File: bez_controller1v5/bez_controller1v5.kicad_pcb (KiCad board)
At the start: 4 copper layers, 130 x 65 mm, 88 parts, among them J1 Conn_01x03_Male, J10 Conn_01x07_Socket, J11 Conn_01x03_Male, J12 Conn_01x03_Male, J13 USB_B_Mini, J14 PPTC041LGBN-RC, J15 Conn_01x03_Male, J16 MOLEX_Conn_Button, J17 MOLEX_Conn_Button, J2 Conn_01x03_Male, J3 Conn_01x03_Male, J4 Screw_Terminal_01x02, J5 Conn_01x03_Male, J6 Conn_01x03_Male, J7 Conn_01x03_Male, J8 JTAG Conn_01x06_Male, J9 Conn_01x09_Socket, U10 USBLC6-4SC6, U11 74LVC2G241, U12 74LVC2G241, U2 74LVC2G241, U3 74LVC2G241, U4 LF50ABV_TO220, U5 LD1117AS33TR_SOT223, U6 INA180A1, U7 STM32F446RETx, U8 74LVC2G241, U9 74LVC2G241, Y1 8MHz

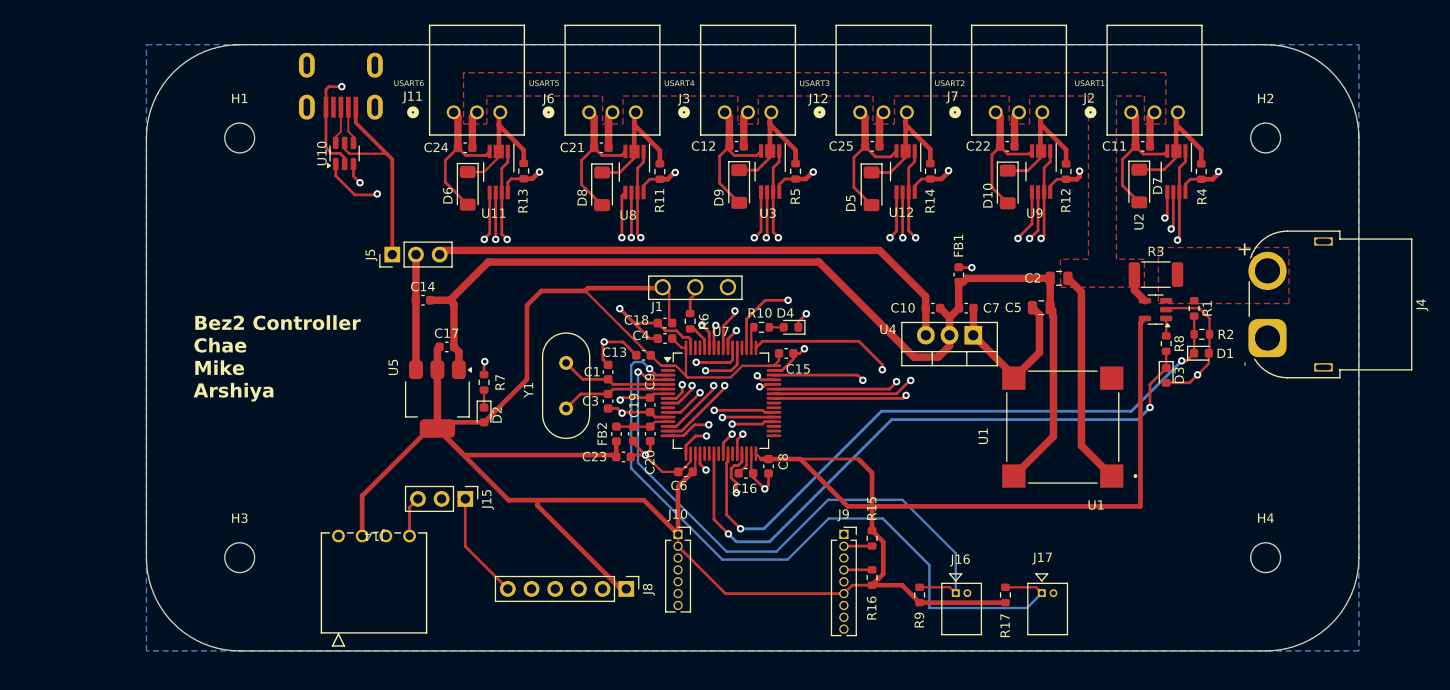
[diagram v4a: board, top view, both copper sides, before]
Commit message: Shortened size of backup board in case we need to reorder
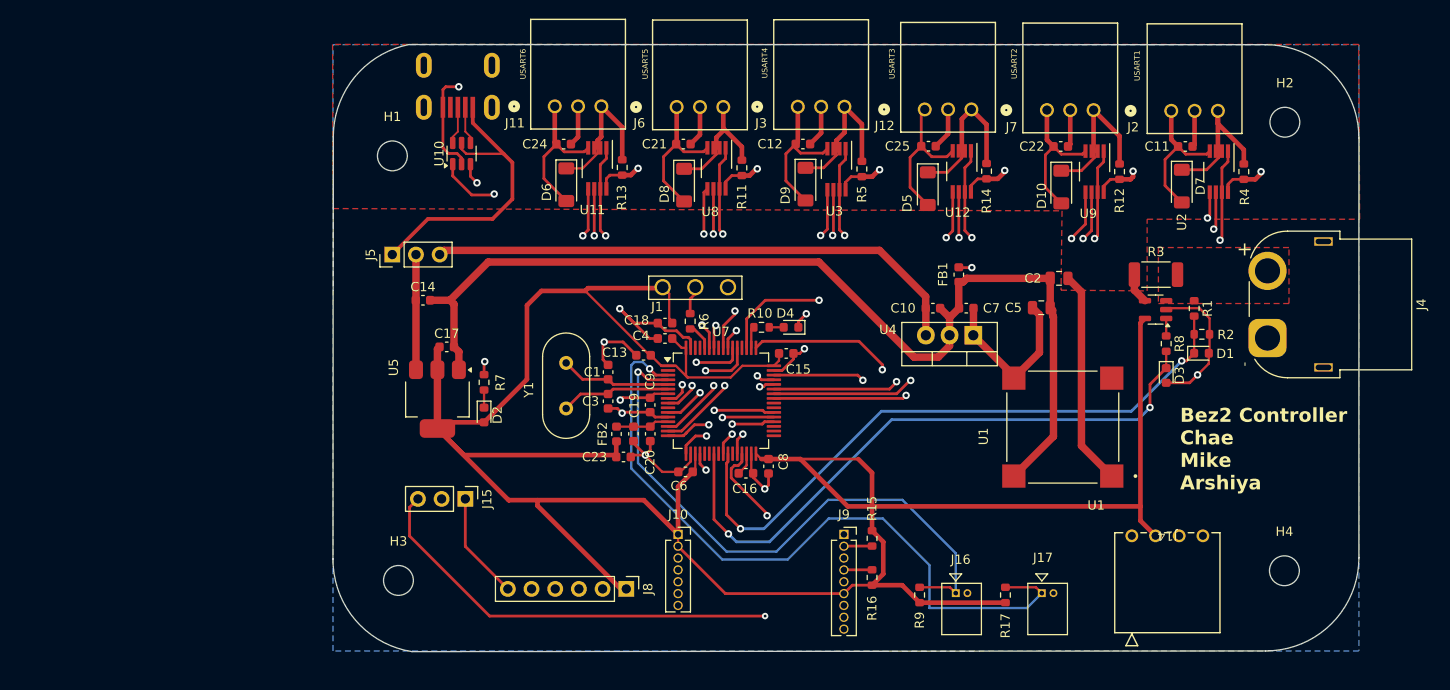
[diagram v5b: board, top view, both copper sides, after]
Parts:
- moved J14 85.1 mm to (189.4, 95.7)
- moved H3 17.2 mm to (110.8, 100.4)
- moved H1 16.5 mm to (110.1, 54.9)
- moved J13 12.5 mm to (117.1, 47.1)
- moved U10 12.5 mm to (117.5, 54.7)
- moved J11 10.9 mm to (127.5, 49.6)
- moved C24 10.6 mm to (128.5, 53.7)
- moved U11 10.6 mm to (132.1, 56.3)
- moved D6 10.6 mm to (128.8, 58.0)
- moved R13 10.6 mm to (134.8, 56.2)
- moved J6 9.40 mm to (140.6, 49.7)
- moved D8 8.80 mm to (141.4, 58.1)
- moved U8 8.80 mm to (144.9, 56.3)
- moved C21 8.80 mm to (141.3, 53.7)
- moved R11 8.80 mm to (147.6, 56.2)
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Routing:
- net /Screen_SDA: track 4.35 -> 103.1 mm, vias 0 -> 1
- net /USB_D-: track 64.9 -> 52.8 mm
- net +3.3V: track 298.6 -> 287.9 mm
- net /USB_D+: track 63.4 -> 52.9 mm
- net VBUS: track 22.0 -> 31.5 mm
- net /USART5_DIR: track 31.0 -> 23.3 mm
- net /Screen_SCL: track 61.3 -> 55.3 mm
- net /USART6_DIR: track 48.4 -> 42.5 mm
- net /USART2_TX: track 53.5 -> 59.3 mm
- net /USART2_RX: track 53.7 -> 59.4 mm
- net /USART2_DIR: track 58.0 -> 63.7 mm
- net /USART3_RX: track 36.0 -> 40.8 mm
- net /USART3_DIR: track 41.4 -> 46.1 mm
- net /USART3_TX: track 28.6 -> 33.3 mm
- net /USART1_DIR: track 66.0 -> 70.5 mm
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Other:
- board size 130 x 65 mm -> 110 x 65.1 mm

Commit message: Smaller board, changed header back to male, optimized some stuff
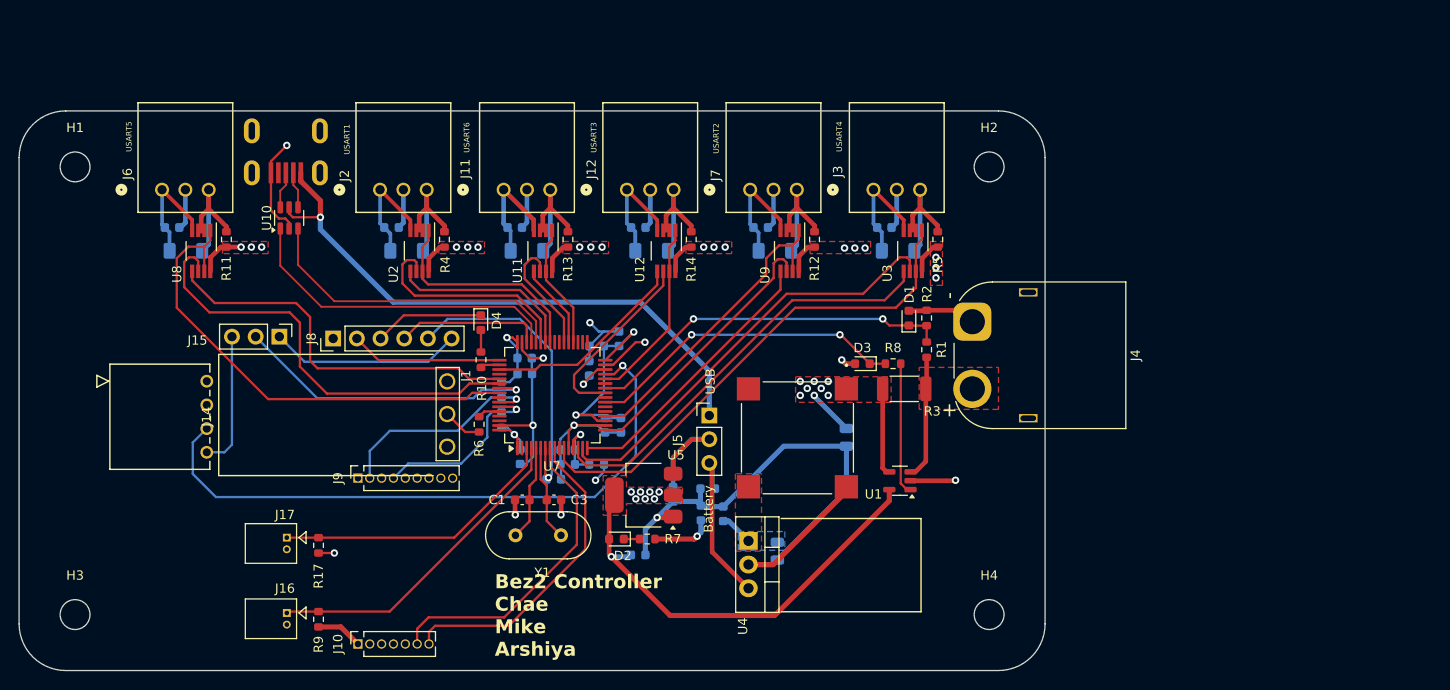
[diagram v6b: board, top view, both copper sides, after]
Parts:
- C10, C11, C12, C13, C14, C15, C16, C17, C18, C19, C2, C20, C21, C22, C23, C24, C25, C4, C5, C6, C7, C8, C9, D10, D5, D6, D7, D8, D9, FB1, FB2, R15, R16: moved to B.Cu
- J4: footprint Connector_AMASS:AMASS_XT60PW-F_1x02_P7.20mm_Horizontal -> Connector_AMASS:AMASS_XT60PW-M_1x02_P7.20mm_Horizontal
- moved J14 100.6 mm to (90.2, 79.1), turned to 90 degrees
- moved U2 86.1 mm to (113.0, 65.1)
- moved R4 86.0 mm to (115.7, 63.9)
- moved C11 85.6 mm to (110.0, 62.6)
- moved J2 85.3 mm to (108.8, 58.5)
- moved D7 83.4 mm to (111.7, 65.1), turned to 180 degrees
- moved J17 81.2 mm to (98.8, 95.8), turned to -90 degrees
- moved R17 73.8 mm to (102.2, 96.7)
- moved J16 71.8 mm to (98.8, 103.9), turned to -90 degrees
- moved R9 64.5 mm to (102.2, 104.6)
- moved U8 55.9 mm to (89.6, 65.1)
- moved J6 55.9 mm to (85.4, 58.5)
- moved R11 55.8 mm to (92.3, 63.9)
- moved C21 55.5 mm to (86.5, 62.6)
- moved D8 53.9 mm to (88.0, 65.1), turned to 180 degrees
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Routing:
- net +3.3V: track 287.9 -> 96.8 mm, vias 0 -> 14
- net /Screen_SDA: track 103.1 -> 14.6 mm, vias 1 -> 0
- net /PWR_GND: track 111.7 -> 64.9 mm, vias 0 -> 1
- net /USART1_DIR: track 70.5 -> 23.8 mm, vias 2 -> 0
- net +5V: track 88.2 -> 41.5 mm, vias 6 -> 18
- net /GPIO2: track 77.1 -> 30.8 mm, vias 1 -> 0
- net /USART1_TX: track 62.2 -> 19.9 mm, vias 2 -> 0
- net /USART1_RX: track 63.9 -> 23.7 mm, vias 2 -> 0
- net /TCK: track 56.2 -> 16.2 mm, vias 1 -> 0
- net /TMS: track 52.5 -> 15.7 mm, vias 1 -> 0
- net VBUS: track 31.5 -> 65.4 mm, vias 0 -> 1
- net /V_shunt_read: track 67.5 -> 34.3 mm
- net /USART6_TX: track 41.0 -> 9.14 mm, vias 2 -> 0
- net /USART2_DIR: track 63.7 -> 33.3 mm, vias 2 -> 0
- net /USART2_RX: track 59.4 -> 29.0 mm, vias 2 -> 0
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- added copper zone on F.Cu, net +3.3V
- added copper zone on In1.Cu, net +3.3V
- added copper zone on F.Cu, net +5V
- added copper zone on B.Cu, net +6V
- added copper zone on F.Cu, net +6V
- added copper zone on In1.Cu, net /post_shunt_12v
- added copper zone on In2.Cu, net GND
- removed copper zone on B.Cu, net GND
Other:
- board size 110 x 65.1 mm -> 110 x 60 mm
- board text added: "Battery"
- board text added: "USB"
- board text removed: "U1"

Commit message: increased motor protection diode to 6.2 V
removed boot loader button

added a 5pin jst connection using same i2c connection as screen Please enter the commit message for your changes. Lines starting
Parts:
- D10, D5, D6, D7, D8, D9: value BZV55B5V1 -> BZV55B6V2
- J1: value Conn_01x03_Male -> B5B-PH-K-S; footprint KiCad:BootloaderButton -> Connector_JST:JST_PH_B5B-PH-K_1x05_P2.00mm_Vertical
- moved J1 17.7 mm to (102.5, 89.5), turned to 180 degrees
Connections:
- J1 pad 1: +3.3V -> GND
- J1 pad 2: Net-(J1-Pin_2) -> +3.3V
- J1 pad 3: GND -> /Screen_SCL
- R6 pad 1: Net-(J1-Pin_2) -> GND
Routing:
- net /Screen_SDA: track 14.6 -> 20.6 mm
- net Net-(J1-Pin_2): track 4.22 -> 0.00 mm
- net /Screen_SCL: track 68.4 -> 71.2 mm
- net GND: track 172.9 -> 175.4 mm

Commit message: Made some fixes
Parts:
- added J18: B5B-PH-K-S, Connector_JST:JST_PH_B5B-PH-K_1x05_P2.00mm_Vertical, F.Cu at (95.7, 90.1)
- moved J1 1.08 mm to (101.6, 90.1), turned to 90 degrees
- moved R6 0.38 mm to (119.4, 83.3)
- moved D5 0.30 mm to (137.9, 65.4)
- moved D6 0.20 mm to (124.5, 65.3)
- moved D10 0.20 mm to (151.2, 65.3)
- moved D9 0.20 mm to (164.3, 65.3)
- moved D8 0.10 mm to (88.0, 65.2)
- moved D7 0.10 mm to (111.7, 65.2)
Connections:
- J1 pad 2: +3.3V -> /power
- J1 pad 5: unconnected-(J1-Pin_5-Pad5) -> /FootGPIO1
- U7 pad 57: unconnected-(U7-PB5-Pad57) -> /FootGPIO2
- U7 pad 61: unconnected-(U7-PB8-Pad61) -> /FootGPIO1
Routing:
- net /power: track 14.4 -> 73.2 mm
- net /FootGPIO2: track 0.00 -> 26.4 mm
- net /FootGPIO1: track 0.00 -> 20.6 mm
- net /Screen_SDA: track 20.6 -> 24.0 mm
- net /Screen_SCL: track 71.2 -> 71.9 mm
- net /USART5_RX: track 47.4 -> 46.8 mm
- net /USART5_DIR: track 52.4 -> 51.8 mm
